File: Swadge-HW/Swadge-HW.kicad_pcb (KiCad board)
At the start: 2 copper layers, 88 parts, among them J1 SAO, J3 PGM, P1 USB_C_Plug_USB2.0, Q1 Q_PMOS_GSD, SW1 YTS-D003-1A, SW2 YTS-D003-1A, SW3 YTS-D003-1A, SW4 YTS-D003-1A, SW5 YTS-D003-1A, SW6 YTS-D003-1A, SW7 B3FS-4002P, SW8 B3FS-4002P, SW9 SW_SPDT_1825232-1, U1 ESP32-S2-MINI-1, U2 RB017A1505A, U3 MT3410, U5 RB017A1505A_Connector, U6 LSM6DSL, U7 GENERIC_LDO_2.8, U9 QMC6308

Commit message: Reset PCB
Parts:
- removed A1: ~, Swadge_Parts:Ichthys
- removed H1, H2, H3: MountingHole, Swadge_Parts:MountingHole_3.2mm_M3
- removed J3: PGM, Swadge_Parts:PinHeader_1x05_P2.54mm_Vertical
- removed LS1, LS2: Buzzer, Swadge_Parts:Buzzer_12.5x7.5
- removed R10, R11: 3.3kΩ, Swadge_Parts:R_0603_1608Metric
- removed R23: 10Ω, Swadge_Parts:R_0603_1608Metric
- removed U4: ~, Swadge_Parts:Touch_Teeth_5b
- added C18: 0.39uF, Swadge_Parts:C_0603_1608Metric, F.Cu at (236.5, 89.4)
- added J2: PJ-307C, Swadge_Parts:PJ-307C, F.Cu at (107.1, 144.8)
- added R9: 20kΩ, Swadge_Parts:R_0603_1608Metric, F.Cu at (244.5, 81.9)
- added U8: FM8002A, Swadge_Parts:SOP-8_3.9x4.9mm_P1.27mm, F.Cu at (210.7, 72.4)
- C14: value 0.1μF -> 1μF
- C15: value 22μF -> 1μF
- R5: value 10Ω -> 20kΩ
- R6: value 33Ω -> 20kΩ
- U9: value QMC6308 -> INGHAi_GSPK2307P-8R1W; footprint Swadge_Parts:BGA-4-.83x.83-EDGE -> Swadge_Parts:INGHAi GSPK2308P-8R0.5W
- moved C19 159.8 mm to (240.5, 69.3)
- moved R4 159.8 mm to (244.5, 69.3)
- moved R24 150.1 mm to (248.5, 71.8)
- moved R25 150.1 mm to (248.5, 74.4)
- moved R26 150.1 mm to (248.5, 76.9)
- moved R27 150.1 mm to (248.5, 79.4)
- moved R28 150.1 mm to (248.5, 81.9)
- moved C1 149.4 mm to (232.5, 69.3)
- moved C10 149.4 mm to (236.5, 69.3)
- moved C11 149.4 mm to (236.5, 71.8)
- moved C12 149.4 mm to (236.5, 74.4)
- moved C13 149.4 mm to (236.5, 76.9)
- moved C14 149.4 mm to (236.5, 79.4)
- moved C15 149.4 mm to (236.5, 81.9)
- moved C16 149.4 mm to (236.5, 84.4)
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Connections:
- net LCD18 renamed LCD28
- C14 pad 1: Net-(U9-VDD) -> GND
- C14 pad 2: GND -> Net-(U8-Bypass)
- C15 pad 1: Net-(U9-VDD) -> +3V3
- J1 pad 5: GPIO17 -> GPIO40
- J1 pad 6: GPIO18 -> GPIO42
- R5 pad 1: BZR2 -> +3V3
- R5 pad 2: Net-(LS2-Pad1) -> SPK_SHDN
- R6 pad 1: Net-(U9-VDD) -> Net-(U8-IN-)
- R6 pad 2: +3V3 -> Net-(U8-VO1)
- U1 pad 21: GPIO17 -> SPK
- U1 pad 22: GPIO18 -> SPK_SHDN
- U1 pad 36: BZR1 -> GPIO40
- U1 pad 38: BZR2 -> GPIO42
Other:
- board outline added: 110.5 x 124.7 mm

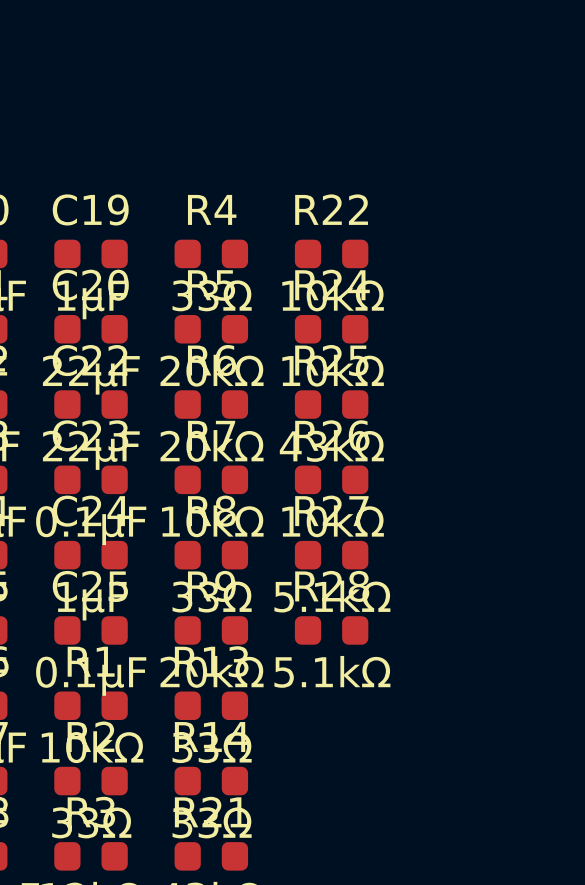
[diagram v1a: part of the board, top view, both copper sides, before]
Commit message: #1 Add ESD resistors to touchpads
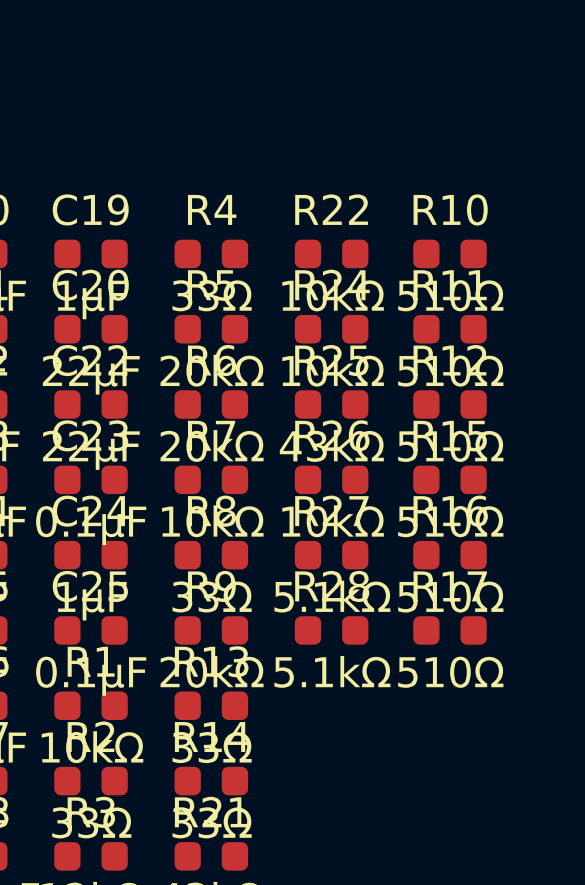
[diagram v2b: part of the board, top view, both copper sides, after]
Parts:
- added R10: 510Ω, Swadge_Parts:R_0603_1608Metric, F.Cu at (252.5, 69.3)
- added R11: 510Ω, Swadge_Parts:R_0603_1608Metric, F.Cu at (252.5, 71.8)
- added R12: 510Ω, Swadge_Parts:R_0603_1608Metric, F.Cu at (252.5, 74.4)
- added R15: 510Ω, Swadge_Parts:R_0603_1608Metric, F.Cu at (252.5, 76.9)
- added R16: 510Ω, Swadge_Parts:R_0603_1608Metric, F.Cu at (252.5, 79.4)
- added R17: 510Ω, Swadge_Parts:R_0603_1608Metric, F.Cu at (252.5, 81.9)

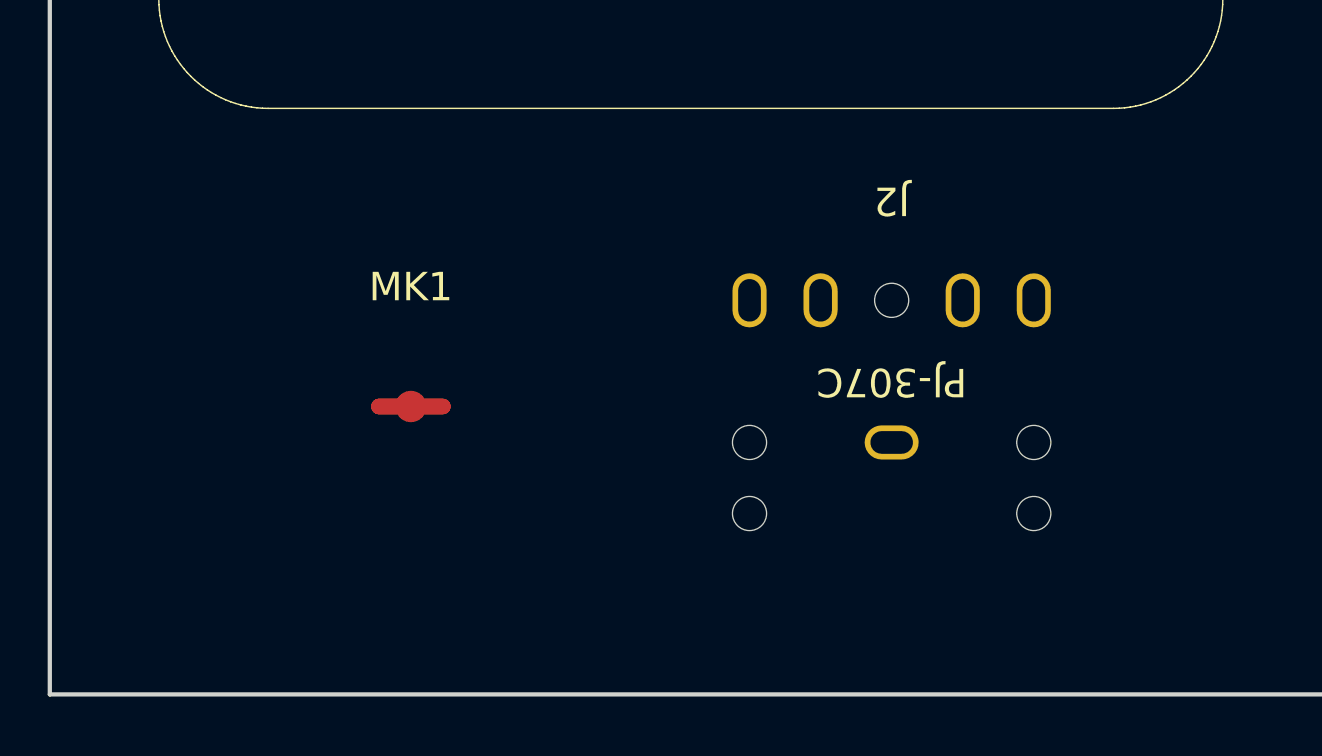
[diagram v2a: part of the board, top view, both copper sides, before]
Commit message: Added volume potentiometer
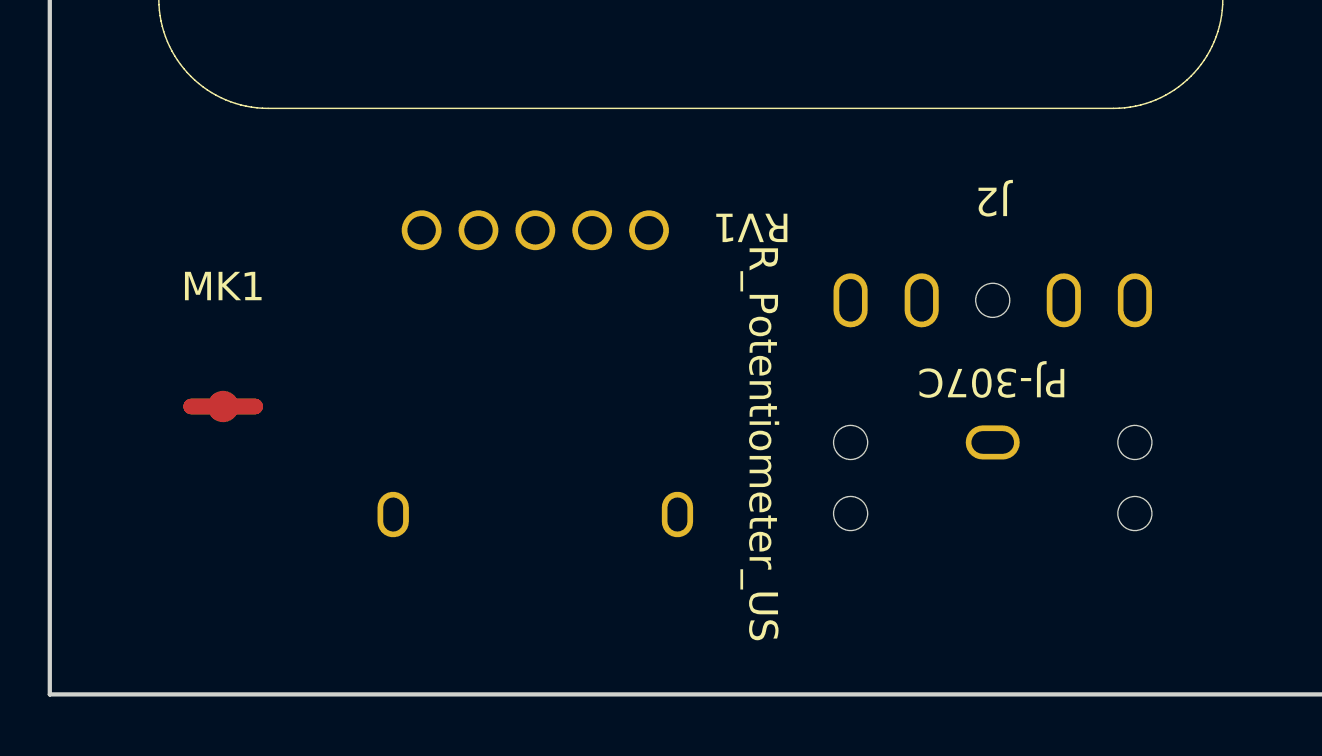
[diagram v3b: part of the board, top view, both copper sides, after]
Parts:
- added RV1: R_Potentiometer_US, Swadge_Parts:RK10J11E0034, F.Cu at (94.5, 144.8)
- moved MK1 6.60 mm to (83.6, 143.5)
- moved J2 3.56 mm to (110.6, 144.8)
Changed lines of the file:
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@@
 	(net 85 "Net-(R16-Pad2)")
 	(net 86 "Net-(R17-Pad2)")
+	(net 87 "unconnected-(RV1-Pad3)")
 	(footprint "Swadge_Parts:C_0603_1608Metric"
 		(layer "F.Cu")
@@
 	(footprint "Swadge_Parts:PJ-307C"
 		(layer "F.Cu")
-		(at 107.085 144.807 180)
+		(at 110.641 144.807 180)
 		(property "Reference" "J2"
 			(at 0 8.5 180)
@@
 		)
 	)
+	(footprint "Swadge_Parts:RK10J11E0034"
+		(layer "F.Cu")
+		(at 94.55 144.842 180)
+		(property "Reference" "RV1"
+			(at -7.62 7.62 180)
+			(unlocked yes)
+			(layer "F.SilkS")
+			(effects
+				(font
+					(size 1 1)
+					(thickness 0.15)
+				)
+			)
+		)
+		(property "Value" "R_Potentiometer_US"
+			(at -8 0 -90)
+			(unlocked yes)
+			(layer "F.SilkS")
+			(effects
+				(font
+					(size 1 1)
+					(thickness 0.15)
+				)
+			)
+		)
+		(property "Footprint" "Swadge_Parts:RK10J11E0034"
+			(at 0 0 360)
+			(layer "F.Fab")
+			(hide yes)
+			(effects
+				(font
+					(size 1.27 1.27)
+					(thickness 0.15)
+				)
+			)
+		)
+		(property "Datasheet" "https://www.lcsc.com/datasheet/lcsc_datasheet_2304140030_ALPSALPINE-RK10J11E002Y_C470644.pdf"
+			(at 0 0 360)
+			(layer "F.Fab")
+			(hide yes)
+			(effects
+				(font
+					(size 1.27 1.27)
+					(thickness 0.15)
+				)
+			)
+		)
+		(property "Description" "RK10J11E0034"
+			(at 0 0 360)
+			(layer "F.Fab")
+			(hide yes)
+			(effects
+				(font
+					(size 1.27 1.27)
+					(thickness 0.15)
+				)
+			)
+		)
+		(property "LCSC" "C470644"
+			(at 0 0 180)
+			(unlocked yes)
+			(layer "F.Fab")
+			(hide yes)
+			(effects
+				(font
+					(size 1 1)
+					(thickness 0.15)
+				)
+			)
+		)
+		(property "Cost @ 2.5k" "0.4924"
+			(at 0 0 180)
+			(unlocked yes)
+			(layer "F.Fab")
+			(hide yes)
+			(effects
+				(font
+					(size 1 1)
+					(thickness 0.15)
+				)
+			)
+		)
+		(property ki_fp_filters "Potentiometer*")
+		(sheetname "Root")
+		(sheetfile "Swadge-HW.kicad_sch")
+		(attr through_hole)
+		(fp_rect
+			(start 5.35 0)
+			(end 7 4)
+			(stroke
+				(width 0.1)
+				(type default)
+			)
+			(fill none)
+			(layer "F.CrtYd")
+		)
+		(fp_rect
+			(start -6 0)
+			(end 5.35 7.5)
+			(stroke
+				(width 0.1)
+				(type default)
+			)
+			(fill none)
+			(layer "F.CrtYd")
+		)
+		(fp_circle
+			(center 0 0)
+			(end 7 0)
+			(stroke
+				(width 0.1)
+				(type default)
+			)
+			(fill none)
+			(layer "F.CrtYd")
+		)
+		(pad "" thru_hole oval
+			(at -5 -2.5 180)
+			(size 1.1 1.6)
+			(drill oval 0.7 1.2)
+			(layers "*.Cu" "*.Mask")
+			(remove_unused_layers no)
+			(thermal_bridge_angle 45)
+		)
+		(pad "" thru_hole circle
+			(at -2 7.5 180)
+			(size 1.4 1.4)
+			(drill 1)
+			(layers "*.Cu" "*.Mask")
+			(remove_unused_layers no)
+		)
+		(pad "" thru_hole circle
+			(at 2 7.5 180)
+			(size 1.4 1.4)
+			(drill 1)
+			(layers "*.Cu" "*.Mask")
+			(remove_unused_layers no)
+		)
+		(pad "" thru_hole oval
+			(at 5 -2.5 180)
+			(size 1.1 1.6)
+			(drill oval 0.7 1.2)
+			(layers "*.Cu" "*.Mask")
+			(remove_unused_layers no)
+			(thermal_bridge_angle 45)
+		)
+		(pad "1" thru_hole circle
+			(at -4 7.5 180)
+			(size 1.4 1.4)
+			(drill 1)
+			(layers "*.Cu" "*.Mask")
+			(remove_unused_layers no)
+			(net 79 "Net-(U8-IN-)")
+			(pinfunction "1")
+			(pintype "passive")
+		)
+		(pad "2" thru_hole circle
+			(at 0 7.5 180)
+			(size 1.4 1.4)
+			(drill 1)
+			(layers "*.Cu" "*.Mask")
+			(remove_unused_layers no)
+			(net 45 "Net-(U8-VO1)")
+			(pinfunction "2")
+			(pintype "passive")
+		)
+		(pad "3" thru_hole circle
+			(at 4 7.5 180)
+			(size 1.4 1.4)
+			(drill 1)
+			(layers "*.Cu" "*.Mask")
+			(remove_unused_layers no)
+			(net 87 "unconnected-(RV1-Pad3)")
+			(pinfunction "3")
+			(pintype "passive+no_connect")
+		)
+		(model "${KIPRJMOD}/../Swadge-Parts/package3d/RK10J1_E.STEP"
+			(offset
+				(xyz 0 0 0)
+			)
+			(scale
+				(xyz 1 1 1)
+			)
+			(rotate
+				(xyz 0 0 0)
+			)
+		)
+	)
 	(footprint "Swadge_Parts:1825232-1"
 		(layer "F.Cu")
@@
 	(footprint "Swadge_Parts:INGHAi_MIC_GMI4013S-2C58DB"
 		(layer "F.Cu")
-		(at 90.171776 143.541776)
+		(at 83.567776 143.541776)
 		(property "Reference" "MK1"
 			(at 0 -4.2 0)

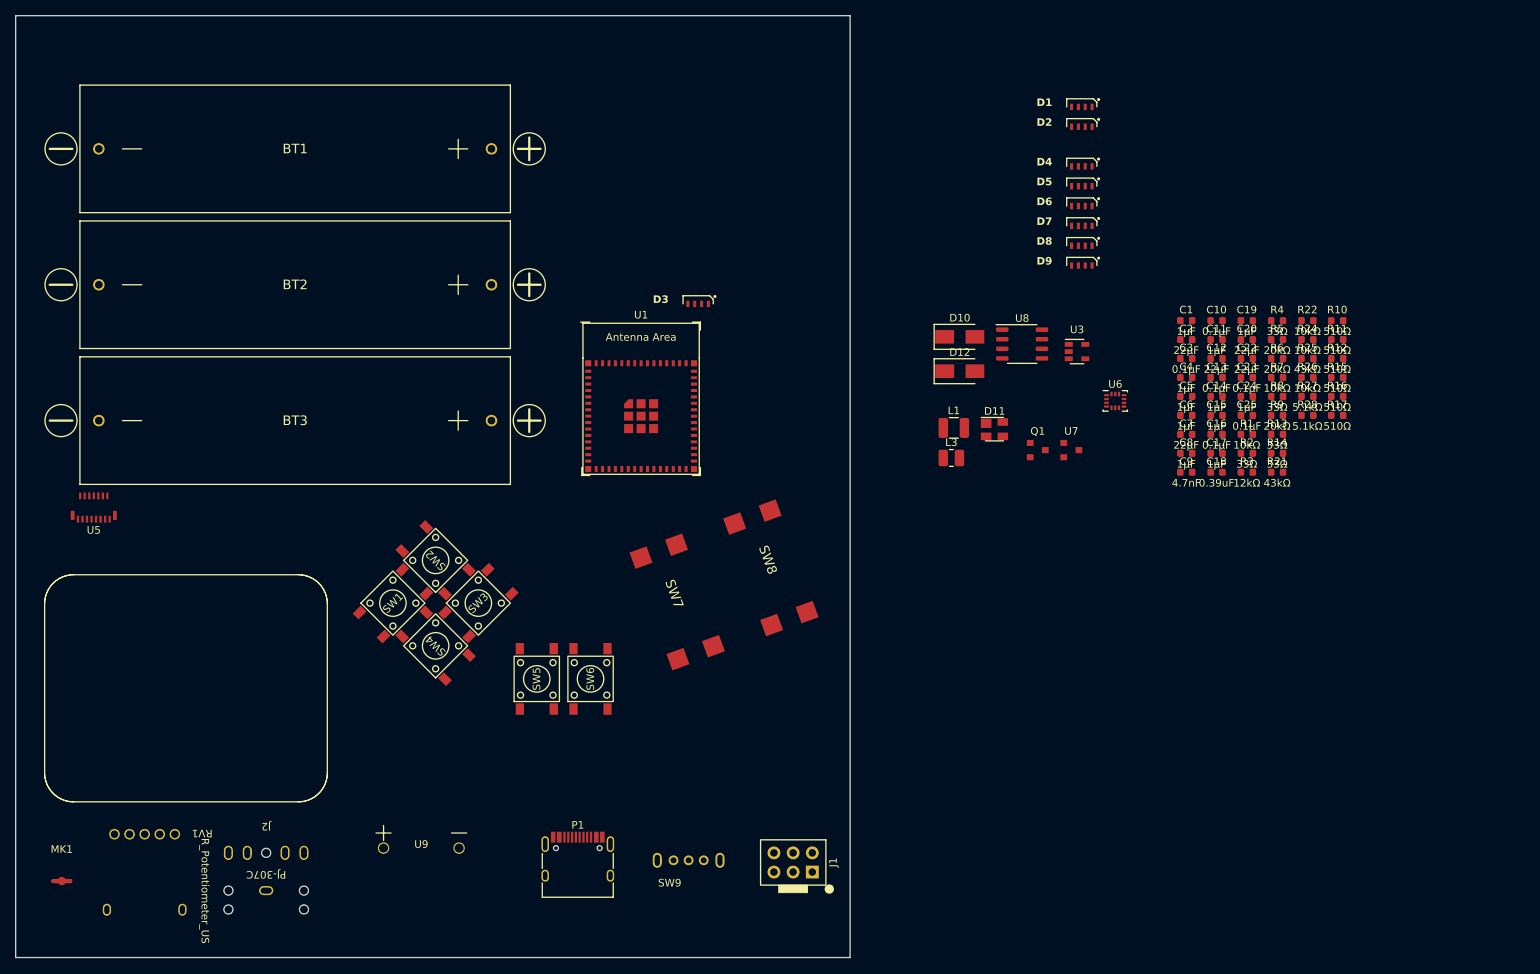
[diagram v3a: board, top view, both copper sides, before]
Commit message: Put touchpad on board
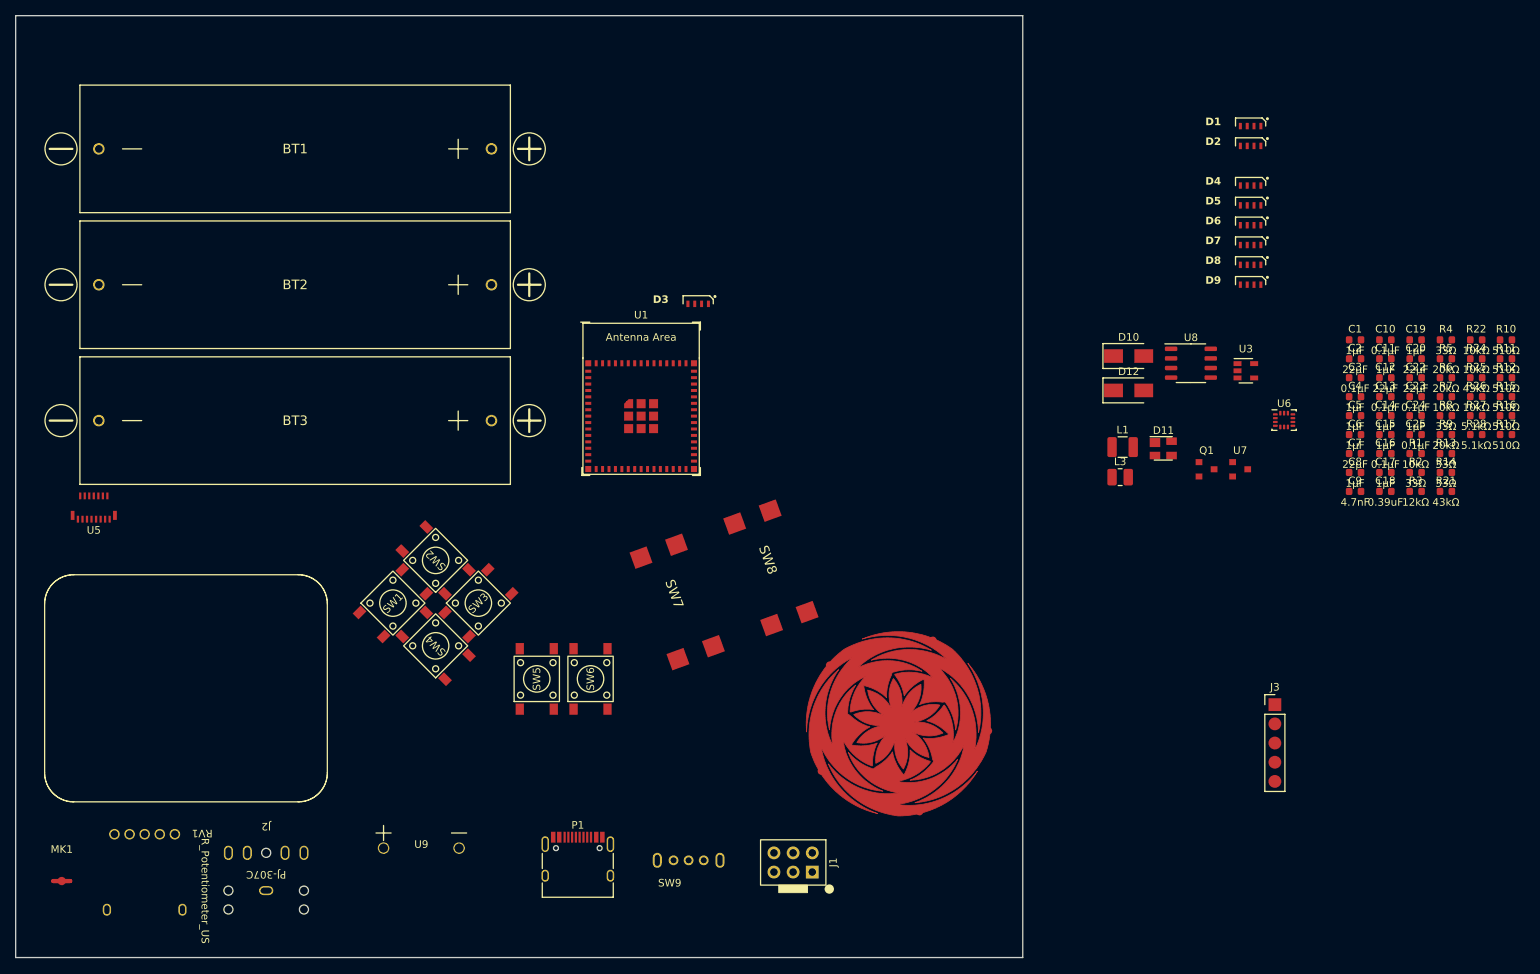
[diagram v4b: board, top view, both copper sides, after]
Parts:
- added J3: PGM, Swadge_Parts:PinHeader_1x05_P2.54mm_Vertical, F.Cu at (244.2, 120.2)
- added U4: ~, Swadge_Parts:Touch_Teeth_5b, F.Cu at (182.1, 110.5)
- moved C10 22.5 mm to (258.8, 71.9)
- moved C11 22.5 mm to (258.8, 74.4)
- moved C12 22.5 mm to (258.8, 76.9)
- moved C13 22.5 mm to (258.8, 79.4)
- moved C14 22.5 mm to (258.8, 81.9)
- moved C15 22.5 mm to (258.8, 84.4)
- moved C16 22.5 mm to (258.8, 86.9)
- moved C17 22.5 mm to (258.8, 89.4)
- moved C18 22.5 mm to (258.8, 92.0)
- moved R10 22.5 mm to (274.8, 71.9)
- moved R11 22.5 mm to (274.8, 74.4)
- moved R12 22.5 mm to (274.8, 76.9)
- moved R15 22.5 mm to (274.8, 79.4)
- moved R16 22.5 mm to (274.8, 81.9)
- moved R17 22.5 mm to (274.8, 84.4)
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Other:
- board size 110.5 x 124.7 mm -> 133.3 x 124.7 mm

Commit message: Add idea of a shape and layout
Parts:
- removed R6: 20kΩ, Swadge_Parts:R_0603_1608Metric
- BT1, BT2, BT3, P1, RV1, SW9, U1: moved to B.Cu
- moved C14 199.9 mm to (60.8, 109.1)
- moved C15 199.9 mm to (60.8, 111.6)
- moved C18 199.9 mm to (60.8, 119.1)
- moved R5 199.9 mm to (68.8, 101.6)
- moved R9 199.9 mm to (68.8, 111.6)
- moved U8 199.9 mm to (35.0, 102.1)
- moved J3 183.3 mm to (71.2, 59.9)
- moved R1 180.8 mm to (82.8, 70.1)
- moved C1 175.6 mm to (79.3, 70.0)
- moved C2 175.6 mm to (79.3, 72.6)
- moved C3 171.6 mm to (83.3, 72.6)
- moved C20 162.0 mm to (101.8, 57.1)
- moved R2 160.8 mm to (105.3, 57.1)
- moved R3 160.8 mm to (105.3, 59.6)
- moved C9 156.4 mm to (101.8, 59.6)
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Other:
- board size 133.3 x 124.7 mm -> 140 x 94.2 mm

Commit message: Added acrylic sausage, SMD pot
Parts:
- added N1: Acrylic Sausage, Swadge_Hotdog:Sausage, F.Cu at (149.8, 126.7)
- RV1: value R_Potentiometer_US -> R_Potentiometer_US_SMD; footprint Swadge_Parts:RK10J11E0034 -> Swadge_Parts:RK10J11R001Y
- moved RV1 2.27 mm to (100.0, 145.1), turned to -60 degrees
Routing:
- added copper zone on F.Cu, net (none)
